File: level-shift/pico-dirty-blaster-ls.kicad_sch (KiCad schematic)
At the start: 14 parts, among them J1 Conn_01x20, J2 Conn_02x05_Odd_Even, J3 Conn_01x04, J4 Conn_02x05_Odd_Even, SW1 SW_Push, U1 TXB0104PW, U6 TS5A63157DBV

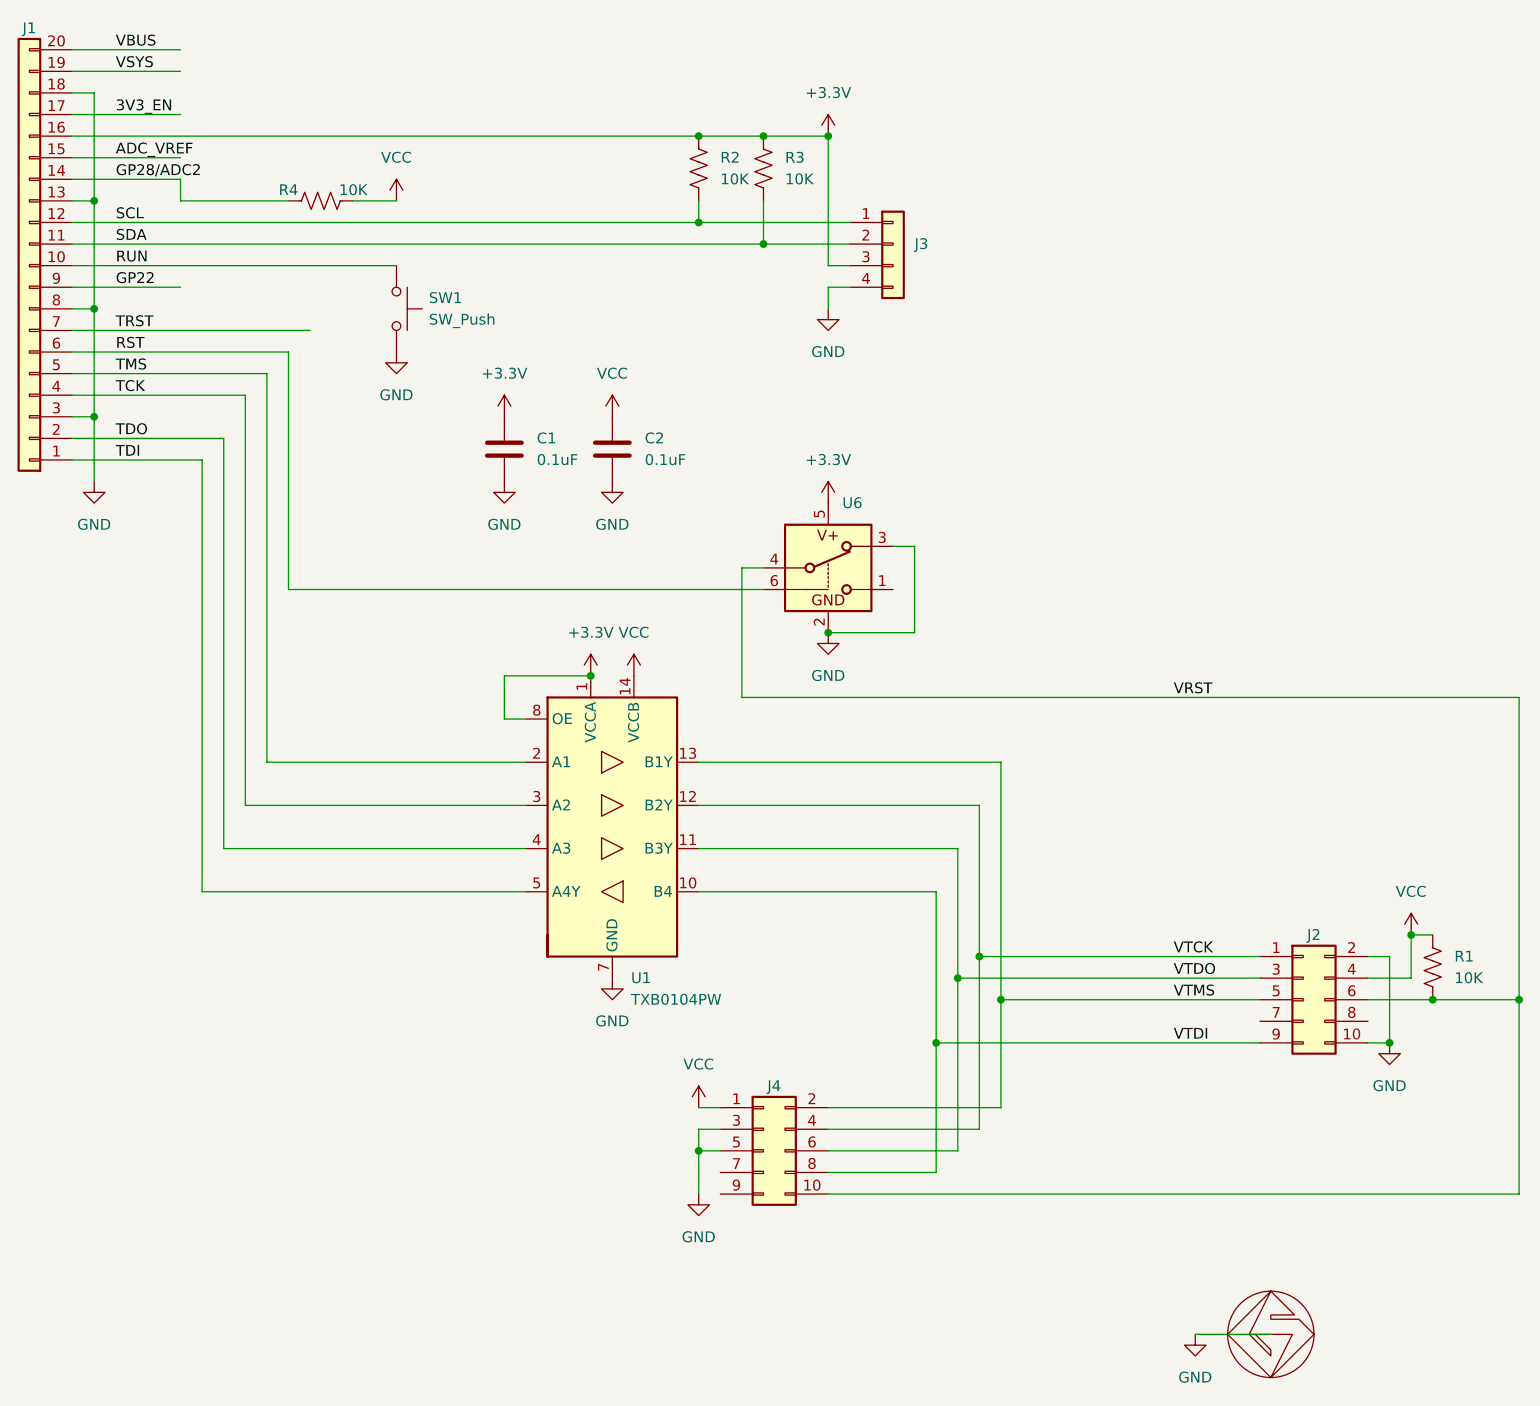
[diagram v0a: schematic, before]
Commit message: changed reset level shift to pass FET
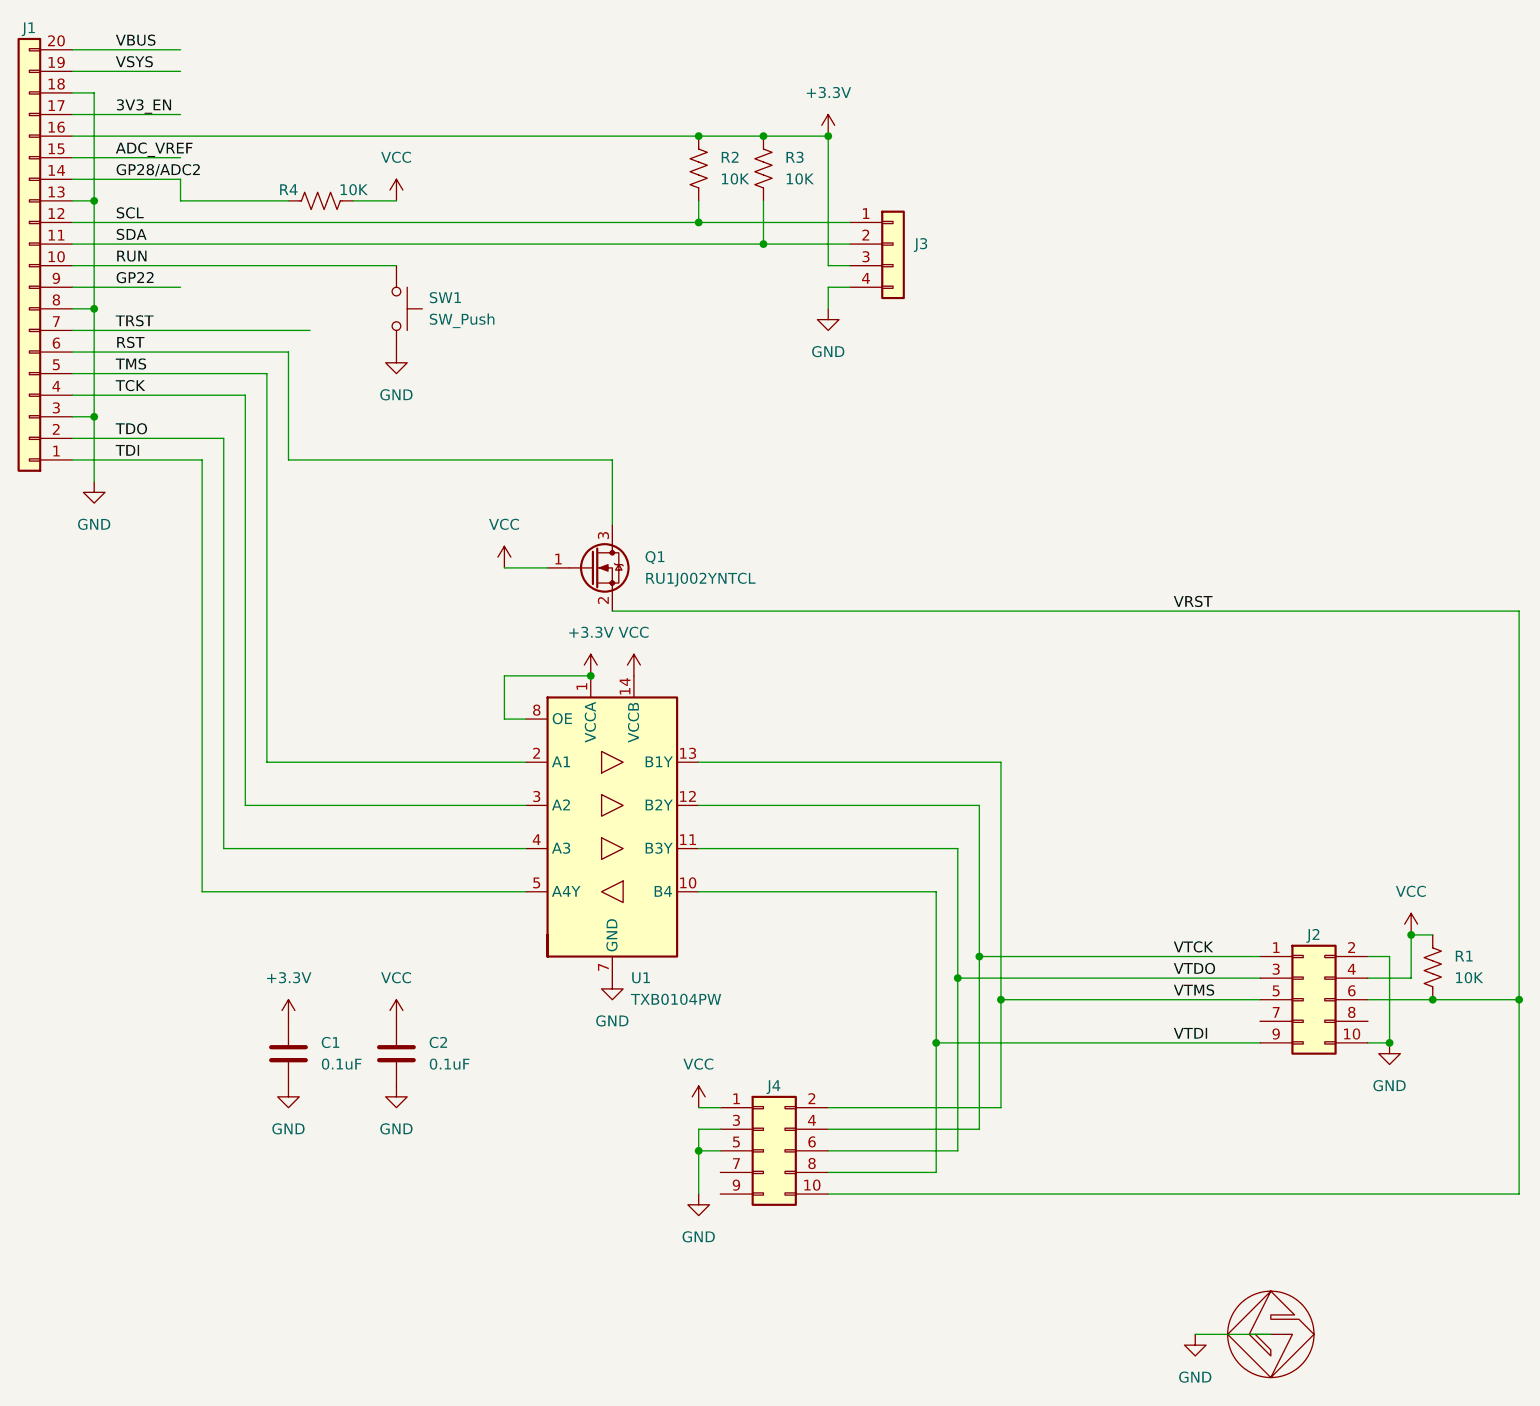
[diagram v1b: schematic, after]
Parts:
- removed U6: TS5A63157DBV, Package_TO_SOT_SMD:SOT-23-6, symbol custom:SPDT-SOT-23
- added Q1: RU1J002YNTCL, Package_TO_SOT_SMD:SOT-323_SC-70, symbol Device:Q_NMOS_Depletion_GSD
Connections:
- net RST: now also Q1.3 (D)
- net VCC: now also Q1.1 (G)
- net VRST: now also Q1.2 (S)
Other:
- moved on the sheet: C1, C2

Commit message: connected vcc on SM, 0402 R on LS
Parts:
- C1, C2: footprint Capacitor_SMD:C_0603_1608Metric_Pad1.08x0.95mm_HandSolder -> Capacitor_SMD:C_0603_1608Metric
- R1, R2, R3, R4: footprint Resistor_SMD:R_0603_1608Metric_Pad0.98x0.95mm_HandSolder -> Resistor_SMD:R_0402_1005Metric
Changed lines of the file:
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@@
       (effects (font (size 1.27 1.27)) (justify left))
     )
-    (property "Footprint" "Resistor_SMD:R_0603_1608Metric_Pad0.98x0.95mm_HandSolder" (at 186.436 136.144 90)
+    (property "Footprint" "Resistor_SMD:R_0402_1005Metric" (at 186.436 136.144 90)
       (effects (font (size 1.27 1.27)) hide)
     )
@@
       (effects (font (size 1.27 1.27)) (justify left))
     )
-    (property "Footprint" "Resistor_SMD:R_0603_1608Metric_Pad0.98x0.95mm_HandSolder" (at 107.696 42.164 90)
+    (property "Footprint" "Resistor_SMD:R_0402_1005Metric" (at 107.696 42.164 90)
       (effects (font (size 1.27 1.27)) hide)
     )
@@
       (effects (font (size 1.27 1.27)) (justify left))
     )
-    (property "Footprint" "Capacitor_SMD:C_0603_1608Metric_Pad1.08x0.95mm_HandSolder" (at 64.4652 149.86 0)
+    (property "Footprint" "Capacitor_SMD:C_0603_1608Metric" (at 64.4652 149.86 0)
       (effects (font (size 1.27 1.27)) hide)
     )
@@
       (effects (font (size 1.27 1.27)))
     )
-    (property "Footprint" "Resistor_SMD:R_0603_1608Metric_Pad0.98x0.95mm_HandSolder" (at 54.864 44.704 90)
+    (property "Footprint" "Resistor_SMD:R_0402_1005Metric" (at 54.864 44.704 90)
       (effects (font (size 1.27 1.27)) hide)
     )
@@
       (effects (font (size 1.27 1.27)) (justify left))
     )
-    (property "Footprint" "Capacitor_SMD:C_0603_1608Metric_Pad1.08x0.95mm_HandSolder" (at 51.7652 149.86 0)
+    (property "Footprint" "Capacitor_SMD:C_0603_1608Metric" (at 51.7652 149.86 0)
       (effects (font (size 1.27 1.27)) hide)
     )
@@
       (effects (font (size 1.27 1.27)) (justify left))
     )
-    (property "Footprint" "Resistor_SMD:R_0603_1608Metric_Pad0.98x0.95mm_HandSolder" (at 100.076 42.164 90)
-      (effects (font (size 1.27 1.27)) hide)
-    )
+    (property "Footprint" "Resistor_SMD:R_0402_1005Metric" (at 100.076 42.164 90)
+      (effects (font (size 1.27 1.27)) hide)
+    )

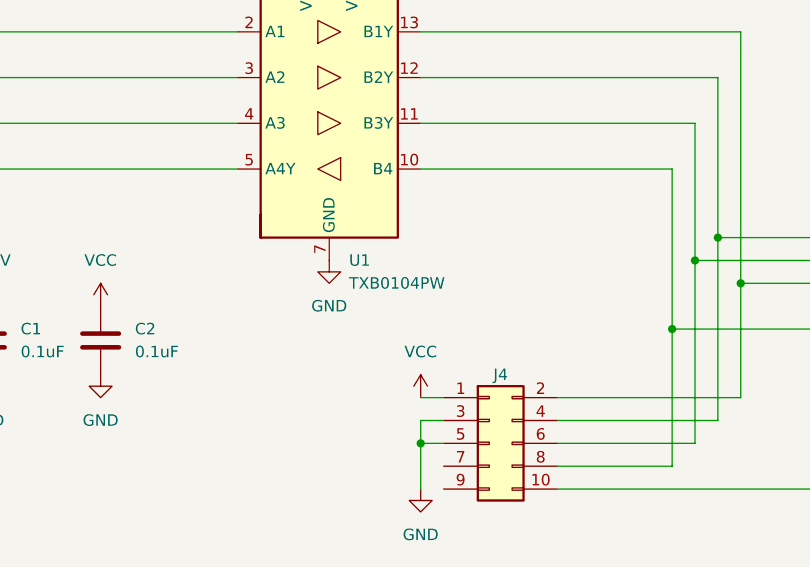
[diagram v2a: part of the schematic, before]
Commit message: fixed part number on level shifter
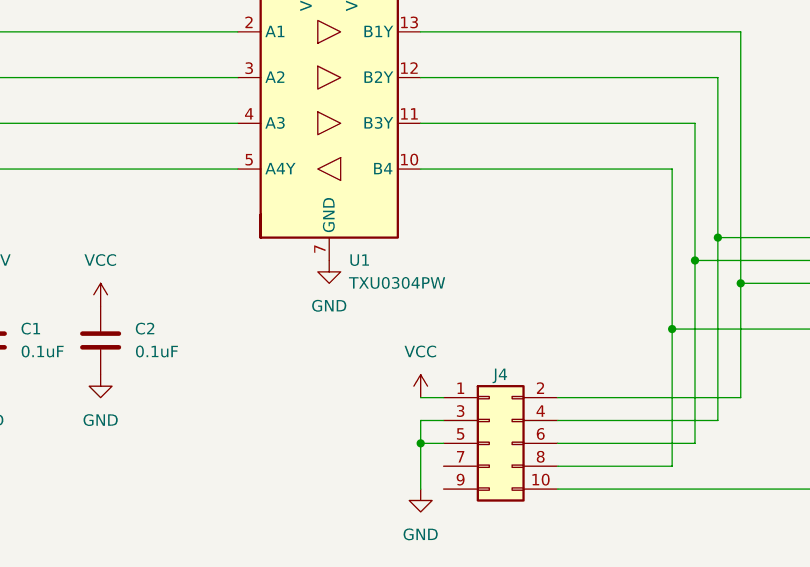
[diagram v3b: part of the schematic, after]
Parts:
- U1: value TXB0104PW -> TXU0304PW
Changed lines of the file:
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@@
       (effects (font (size 1.27 1.27)) (justify left))
     )
-    (property "Value" "TXB0104PW" (at 91.0941 139.7 0)
+    (property "Value" "TXU0304PW" (at 91.0941 139.7 0)
       (effects (font (size 1.27 1.27)) (justify left))
     )
@@
       (effects (font (size 1.27 1.27)) hide)
     )
-    (property "Datasheet" "http://www.ti.com/lit/ds/symlink/txb0104.pdf" (at 91.694 116.967 0)
+    (property "Datasheet" "https://www.ti.com/lit/gpn/TXU0304" (at 91.694 116.967 0)
       (effects (font (size 1.27 1.27)) hide)
     )
